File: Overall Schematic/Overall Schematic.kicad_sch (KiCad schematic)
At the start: 32 parts, among them U12 Spark MAX Motor Controller, U16 Spark MAX Motor Controller, U2 Jetson Nano, U20 Spark MAX Motor Controller, U24 Rev Neo, U25 Rev Neo, U26 Rev Neo, U27 Rev Neo, U28 E-STOP, U29 Power Distribution Panel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

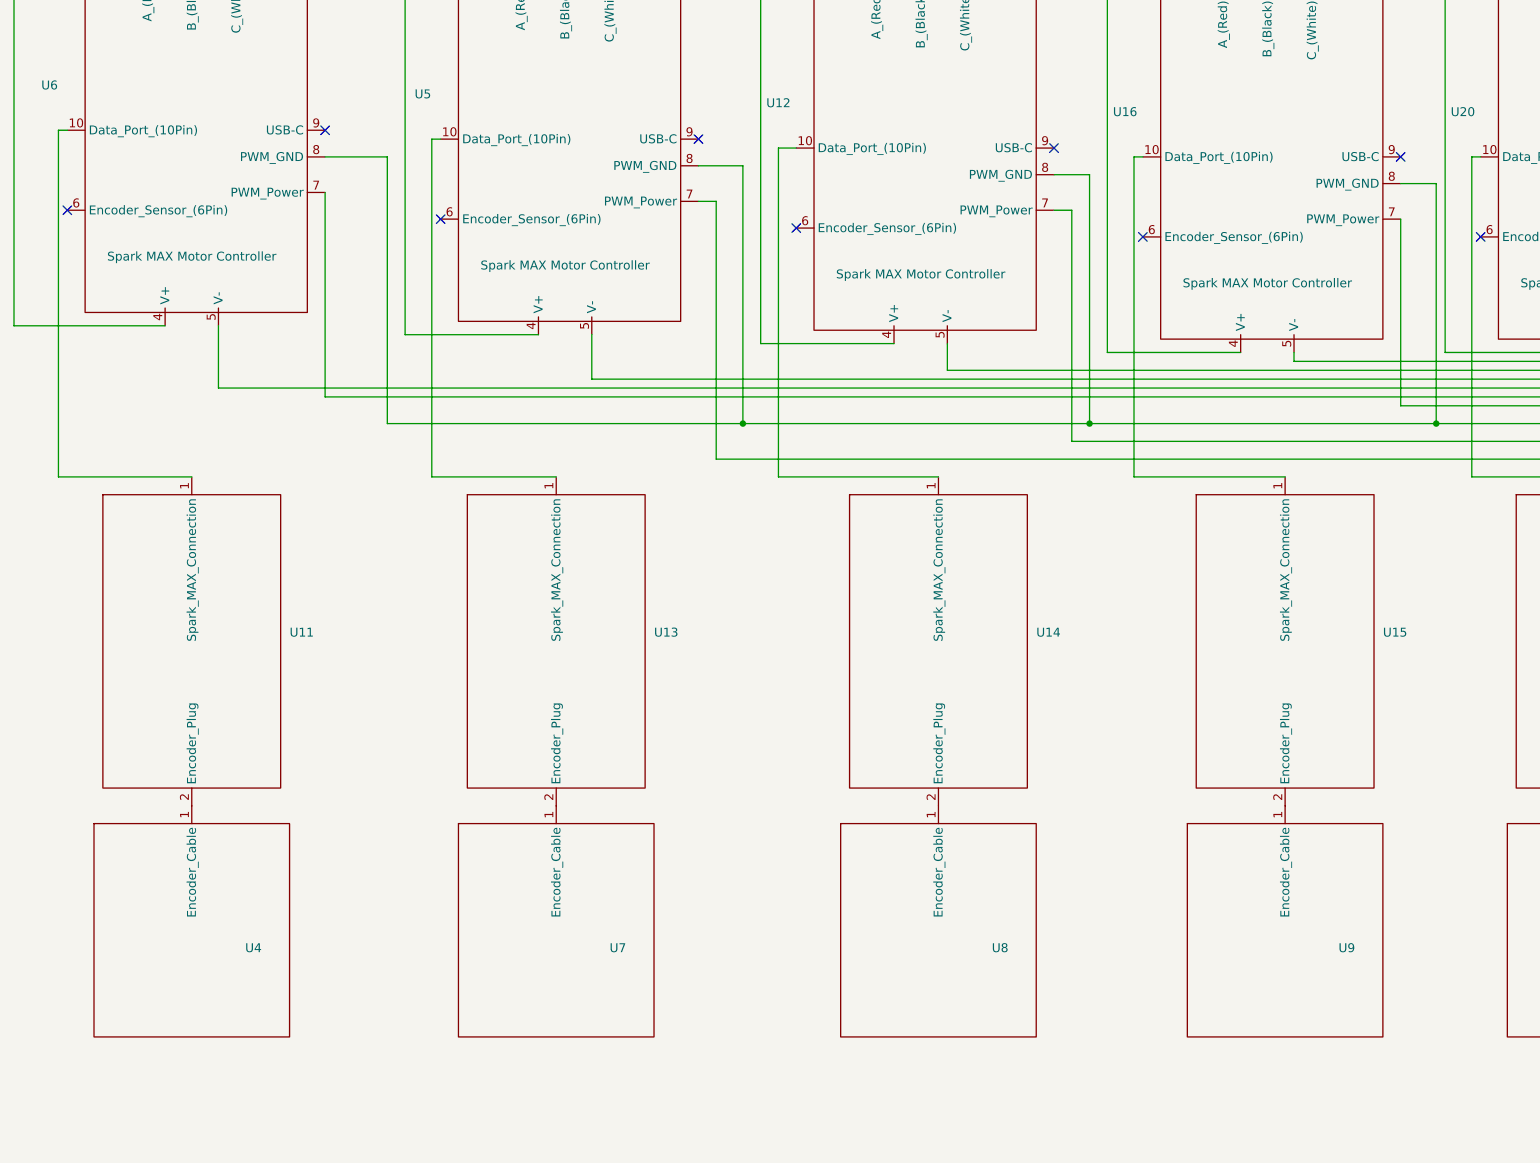
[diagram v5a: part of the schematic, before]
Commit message: Updated controls and overall schematic
Not as many encoders are needed, so they were removed from the schematics.
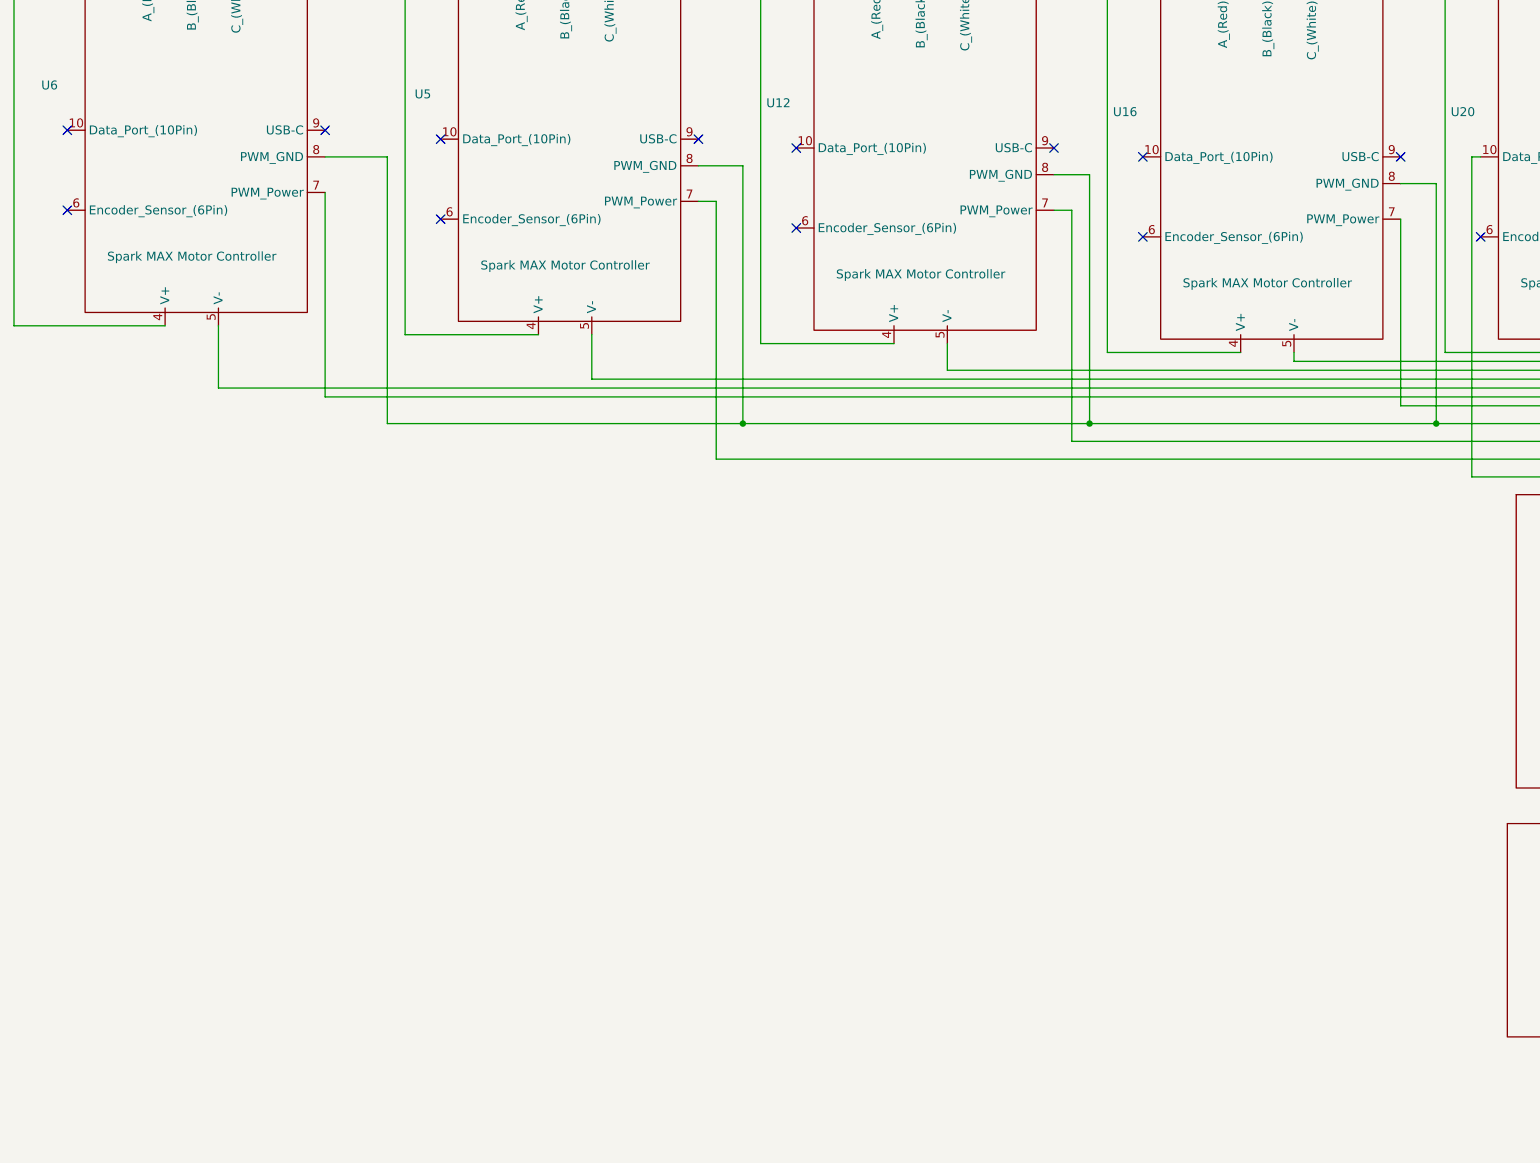
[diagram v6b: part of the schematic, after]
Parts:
- removed U11, U13, U14, U15: ~, symbol Lunabotics 2025-26:Rev_Alternate_Encoder_Adaptor
- removed U4, U7, U8, U9: ~, symbol Lunabotics 2025-26:REV_Through_Bore_Encoder
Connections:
- net at U29. (GRND): no longer 14.8V-5V1. (5V_6A_OUT)
- new net: 14.8V-5V1. (5V_6A_OUT), U29. (GRND)
- no-connect marks 28 -> 32

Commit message: Updated Spark MAX schematic for actual wiring
Also started updating the overall schematic to reflect actual build
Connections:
- net GND: now also U32.9 (PWM_GND); no longer U32.8 (PWM_GND)
- net at U17.1 (Spark_MAX_Connection): now also U20.12 (Data_Port_(10Pin)); no longer U20.10 (Data_Port_(10Pin))
- net at U12.6 (PWM_Power): now also U5.6 (PWM_Power)
- net at U12.7 (PWM_GND): now also U5.7 (PWM_GND)
- net at U12.9 (PWM_GND): now also U16.9 (PWM_GND)
- net at U29. (GRND): no longer 14.8V-5V1. (5V_6A_OUT)
- net at U6.9 (PWM_GND): now also U5.9 (PWM_GND)
- net at U20.6 (PWM_Power): now also U16.6 (PWM_Power)
- net at U20.7 (PWM_GND): now also U16.7 (PWM_GND)
- new net: U12.8 (PWM_Power), U16.8 (PWM_Power)
- new net: 14.8V-5V1. (5V_6A_OUT), U29. (GRND)
- new net: U5.8 (PWM_Power), U6.8 (PWM_Power)
- now unconnected: U2.20 (GPIO), U20.8 (PWM_GND)
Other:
- note removed: "To be connected to microcontroller"

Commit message: Finished updating Overall to match build
Updated Spark MAX and Jetson Nano Symbols
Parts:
- added R1: 120Ω, symbol Device:R
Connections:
- net at U29. (GRND): no longer 14.8V-5V1. (5V_6A_OUT)
- net at U6.6 (PWM_Power): now also R1.2
- net at U6.7 (PWM_GND): now also R1.1
- net at U20.8 (PWM_Power): now also U2.50 (USB_Port), U20.9 (PWM_GND)
- new net: 14.8V-5V1. (5V_6A_OUT), U29. (GRND)
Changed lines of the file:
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@@
 	)
 	(junction
+		(at 372.11 144.78)
+		(diameter 0)
+		(color 0 0 0 0)
+	)
+	(junction
 		(at 378.46 106.68)
 		(diameter 0)
@@
 	(wire
 		(pts
+			(xy 372.11 139.7) (xy 372.11 144.78)
+		)
+		(stroke
+			(width 0)
+			(type default)
+		)
+	)
+	(wire
+		(pts
 			(xy 152.4 161.29) (xy 152.4 167.64)
 		)
@@
 	(wire
 		(pts
+			(xy 114.3 149.86) (xy 114.3 153.67)
+		)
+		(stroke
+			(width 0)
+			(type default)
+		)
+	)
+	(wire
+		(pts
 			(xy 223.52 143.51) (xy 223.52 67.31)
 		)
@@
 	(wire
 		(pts
+			(xy 316.23 139.7) (xy 372.11 139.7)
+		)
+		(stroke
+			(width 0)
+			(type default)
+		)
+	)
+	(wire
+		(pts
 			(xy 462.28 167.64) (xy 462.28 113.03)
 		)
@@
 	(wire
 		(pts
+			(xy 372.11 144.78) (xy 372.11 224.79)
+		)
+		(stroke
+			(width 0)
+			(type default)
+		)
+	)
+	(wire
+		(pts
 			(xy 220.98 138.43) (xy 220.98 64.77)
 		)
@@
 	(wire
 		(pts
+			(xy 114.3 153.67) (xy 119.38 153.67)
+		)
+		(stroke
+			(width 0)
+			(type default)
+		)
+	)
+	(wire
+		(pts
 			(xy 378.46 106.68) (xy 411.48 106.68)
 		)
@@
 	(wire
 		(pts
+			(xy 114.3 146.05) (xy 119.38 146.05)
+		)
+		(stroke
+			(width 0)
+			(type default)
+		)
+	)
+	(wire
+		(pts
 			(xy 509.27 102.87) (xy 515.62 102.87)
 		)
@@
 	(wire
 		(pts
+			(xy 316.23 144.78) (xy 372.11 144.78)
+		)
+		(stroke
+			(width 0)
+			(type default)
+		)
+	)
+	(wire
+		(pts
 			(xy 199.39 95.25) (xy 199.39 109.22)
 		)
@@
 	)
 	(symbol
+		(lib_id "Device:R")
+		(at 119.38 149.86 0)
+		(unit 1)
+		(exclude_from_sim no)
+		(in_bom yes)
+		(on_board yes)
+		(dnp no)
+		(fields_autoplaced yes)
+		(property "Reference" "R1"
+			(at 121.92 148.5899 0)
+			(effects
+				(font
+					(size 1.27 1.27)
+				)
+				(justify left)
+			)
+		)
+		(property "Value" "120Ω"
+			(at 121.92 151.1299 0)
+			(effects
+				(font
+					(size 1.27 1.27)
+				)
+				(justify left)
+			)
+		)
+		(property "Footprint" ""
+			(at 117.602 149.86 90)
+			(effects
+				(font
+					(size 1.27 1.27)
+				)
+				(hide yes)
+			)
+		)
+		(property "Datasheet" "~"
+			(at 119.38 149.86 0)
+			(effects
+				(font
+					(size 1.27 1.27)
+				)
+				(hide yes)
+			)
+		)
+		(property "Description" "Resistor"
+			(at 119.38 149.86 0)
+			(effects
+				(font
+					(size 1.27 1.27)
+				)
+				(hide yes)
+			)
+		)
+		(pin "1"
+		)
+		(pin "2"
+		)
+		(instances
+			(project ""
+				(path "/b876505b-23a1-4d11-8fd1-5d37220464c6"
+					(reference "R1")
+					(unit 1)
+				)
+			)
+		)
+	)
+	(symbol
 		(lib_id "Lunabotics 2025-26:Rev_Neo")
 		(at 95.25 78.74 0)
@@
 		(pin "22"
 		)
+		(pin "47"
+		)
+		(pin "50"
+		)
+		(pin "48"
+		)
+		(pin "49"
+		)
 		(instances
